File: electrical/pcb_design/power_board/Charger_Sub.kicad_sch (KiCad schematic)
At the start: 10 parts

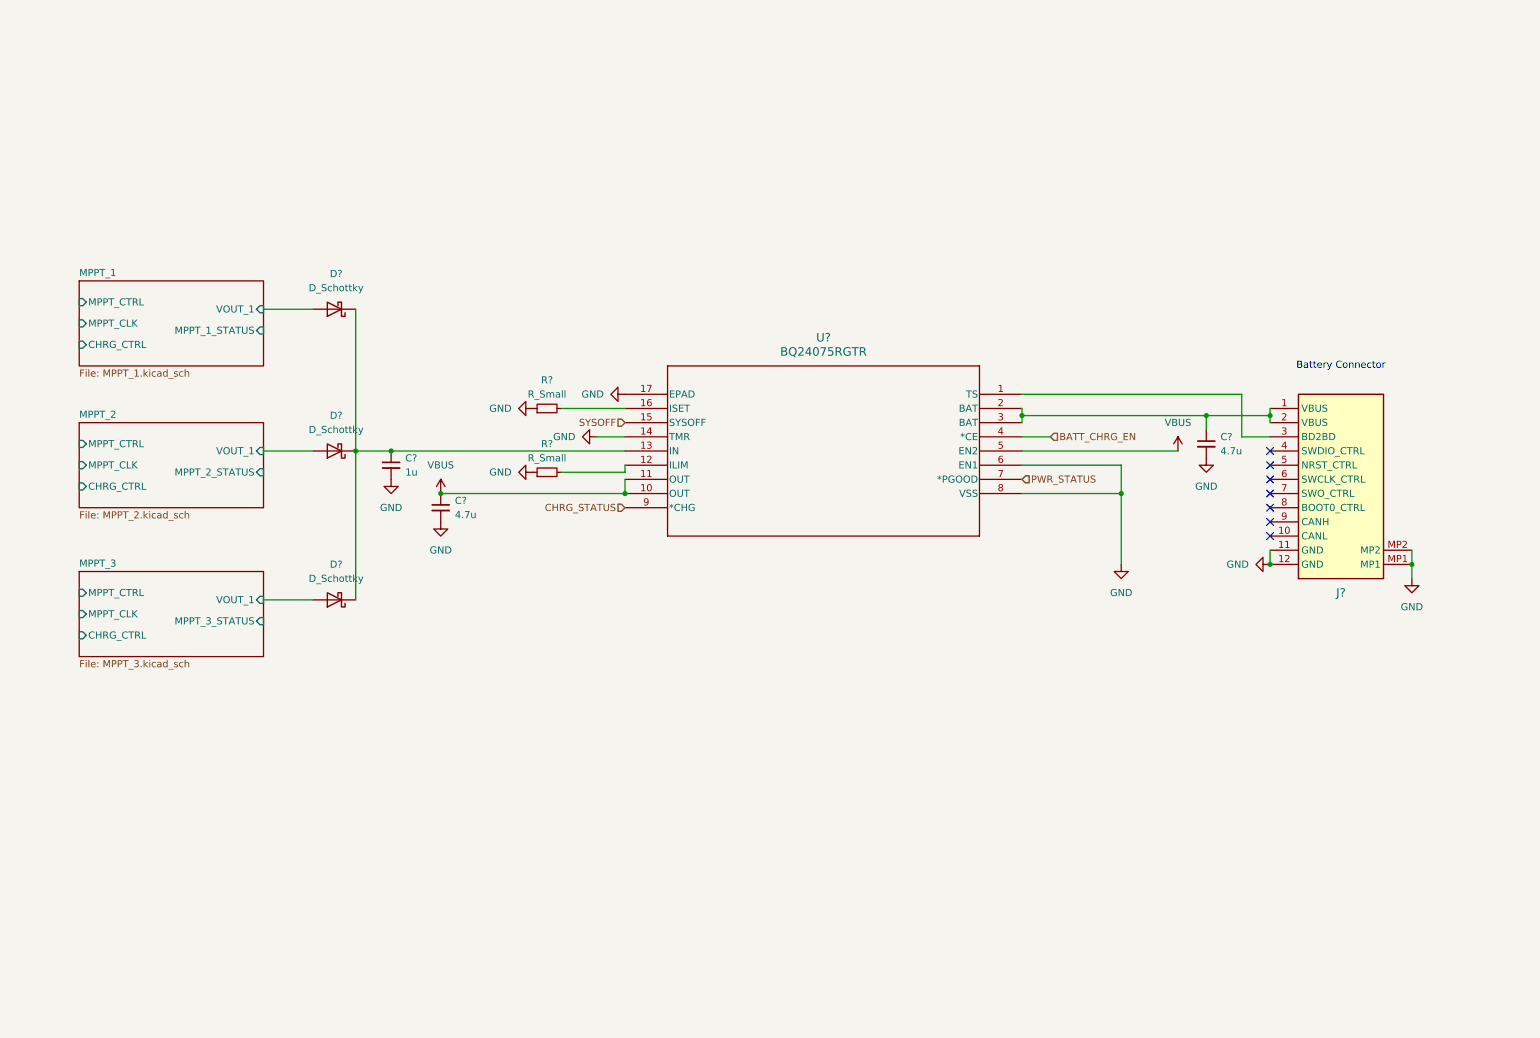
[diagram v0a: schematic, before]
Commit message: power board schematic first draft but missing some resistor and diode specs, and smart mcu pinout
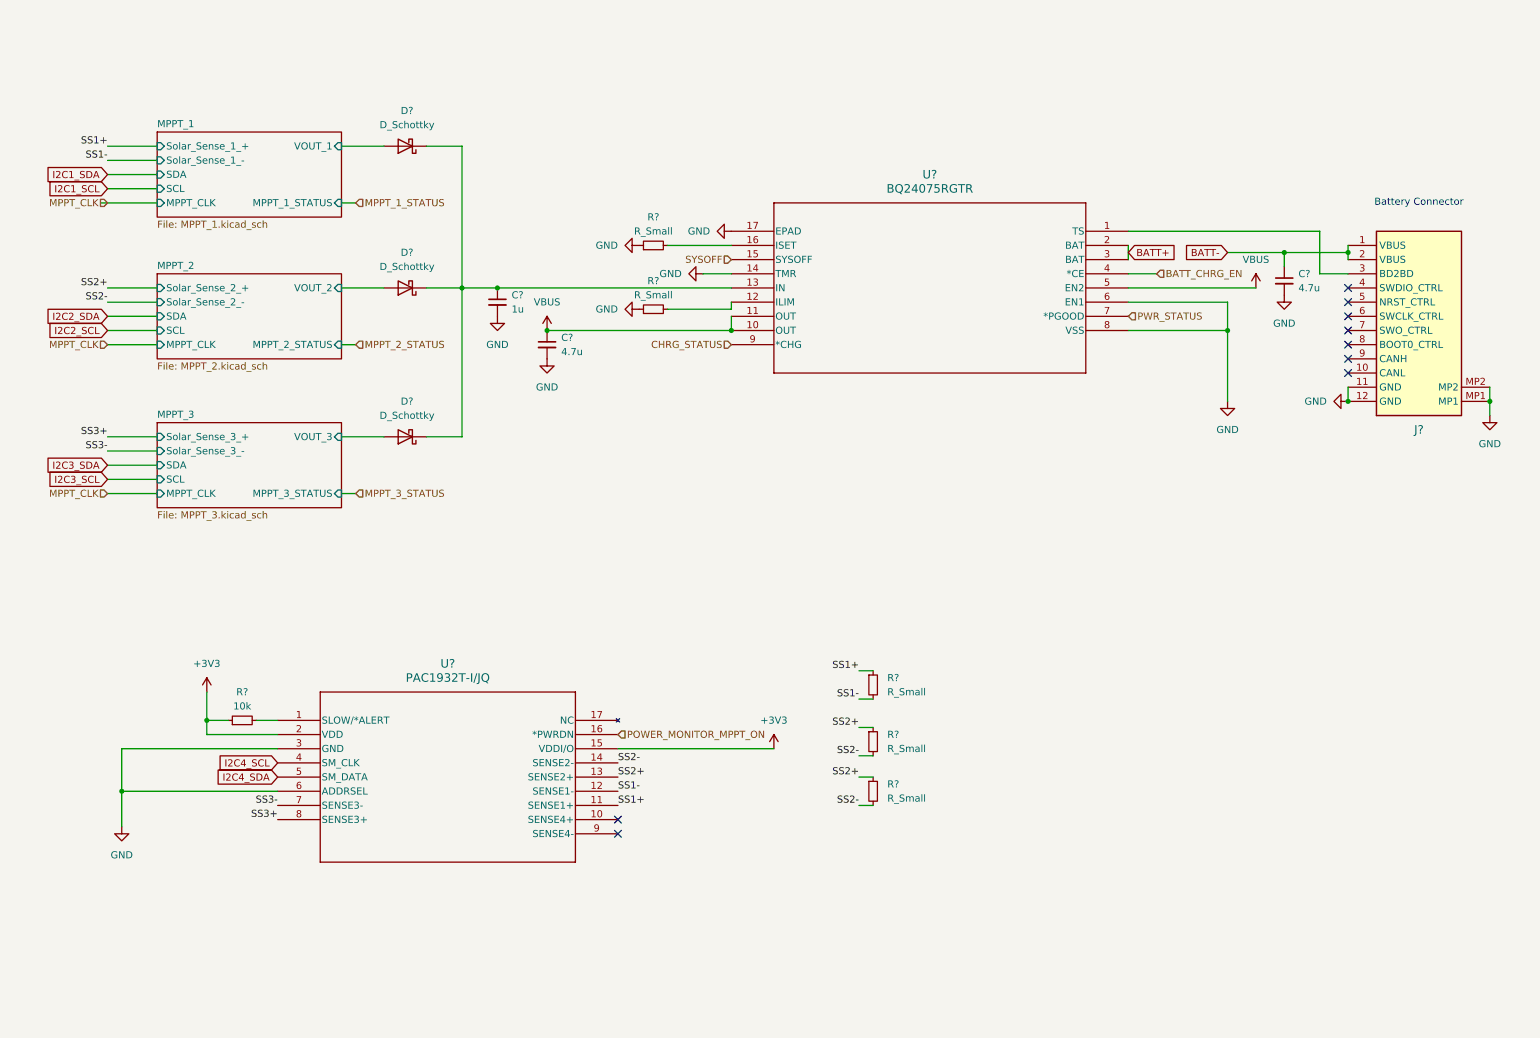
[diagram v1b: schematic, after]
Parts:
- removed D? (x2): D_Schottky, symbol Device:D_Schottky
- added D? (x2): D_Schottky, symbol Device:D_Schottky
- added R? (x3): R_Small, symbol Device:R_Small
- added R?: 10k, symbol Device:R_Small
- added U?: PAC1932T-I/JQ, UQFN16_JQ_MCH, symbol PAC1932:PAC1932T-I_JQ
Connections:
- net GND: now also U?.3 (GND), U?.6 (ADDRSEL)
- net at C?.1, D?.1 (K), U?.13 (IN): now also D?.1 (K), D?.1 (K)
- net BATT-: now reaches C?.1, J?.1 (VBUS), J?.2 (VBUS)
- net BATT-: no longer U?.2 (BAT), U?.3 (BAT)
- new net: R?.2, U?.1 (SLOW/*ALERT)
- new net +3V3: R?.1, U?.15 (VDDI/O), U?.2 (VDD)
- new net BATT+: U?.2 (BAT), U?.3 (BAT)
- new net I2C4_SCL: U?.4 (SM_CLK)
- new net I2C4_SDA: U?.5 (SM_DATA)
- new net MPPT_2/VOUT_2: D?.2 (A)
- new net MPPT_3/VOUT_3: D?.2 (A)
- new net POWER_MONITOR_MPPT_ON: U?.16 (*PWRDN)
- new net SS1+: R?.1, U?.11 (SENSE1+)
- new net SS1-: R?.2, U?.12 (SENSE1-)
- new net SS2+: R?.1, R?.1, U?.13 (SENSE2+)
- new net SS2-: R?.2, R?.2, U?.14 (SENSE2-)
- new net SS3+: U?.8 (SENSE3+)
- new net SS3-: U?.7 (SENSE3-)
- no-connect marks 7 -> 9
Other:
- sheet MPPT_1 ports: added SCL, SDA, Solar_Sense_1_+, Solar_Sense_1_-; removed CHRG_CTRL, MPPT_CTRL
- sheet MPPT_2 ports: added SCL, SDA, Solar_Sense_2_+, Solar_Sense_2_-, VOUT_2; removed CHRG_CTRL, MPPT_CTRL, VOUT_1
- sheet MPPT_3 ports: added SCL, SDA, Solar_Sense_3_+, Solar_Sense_3_-, VOUT_3; removed CHRG_CTRL, MPPT_CTRL, VOUT_1
- moved on the sheet: C?, D?, J?, R?, U?

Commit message: schematic review and some spec-ing
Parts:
- added R?: R_Small, symbol Device:R_Small
- added TP? (x4): ~, symbol Connector:TestPoint_Probe
- R?: value R_Small -> 1.18k
- R?: value R_Small -> 890
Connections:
- net POWER_MONITOR_MPPT_ON is gone; now on net +3V3: U?.16 (*PWRDN)
- net SYSOFF is gone; now on net GND: U?.15 (SYSOFF)
- net MPPT_1/VOUT_1: now also TP?.1
- net MPPT_2/VOUT_2: now also TP?.1
- net MPPT_3/VOUT_3: now also TP?.1
- net SS2+: no longer R?.1
- net SS2-: no longer R?.2
- net SS3+: now also R?.1
- net SS3-: now also R?.2
- net VBUS: now also U?.9 (SENSE4-), R?.2; no longer U?.10 (OUT), U?.11 (OUT)
- net at C?.1, D?.1 (K), D?.1 (K)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: now also TP?.1
- net Load+: now reaches U?.10 (SENSE4+)
- net Load+: now also U?.10 (OUT), U?.11 (OUT), R?.1
- no-connect marks 9 -> 7
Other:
- sheet MPPT_1 ports: added none; removed MPPT_CLK

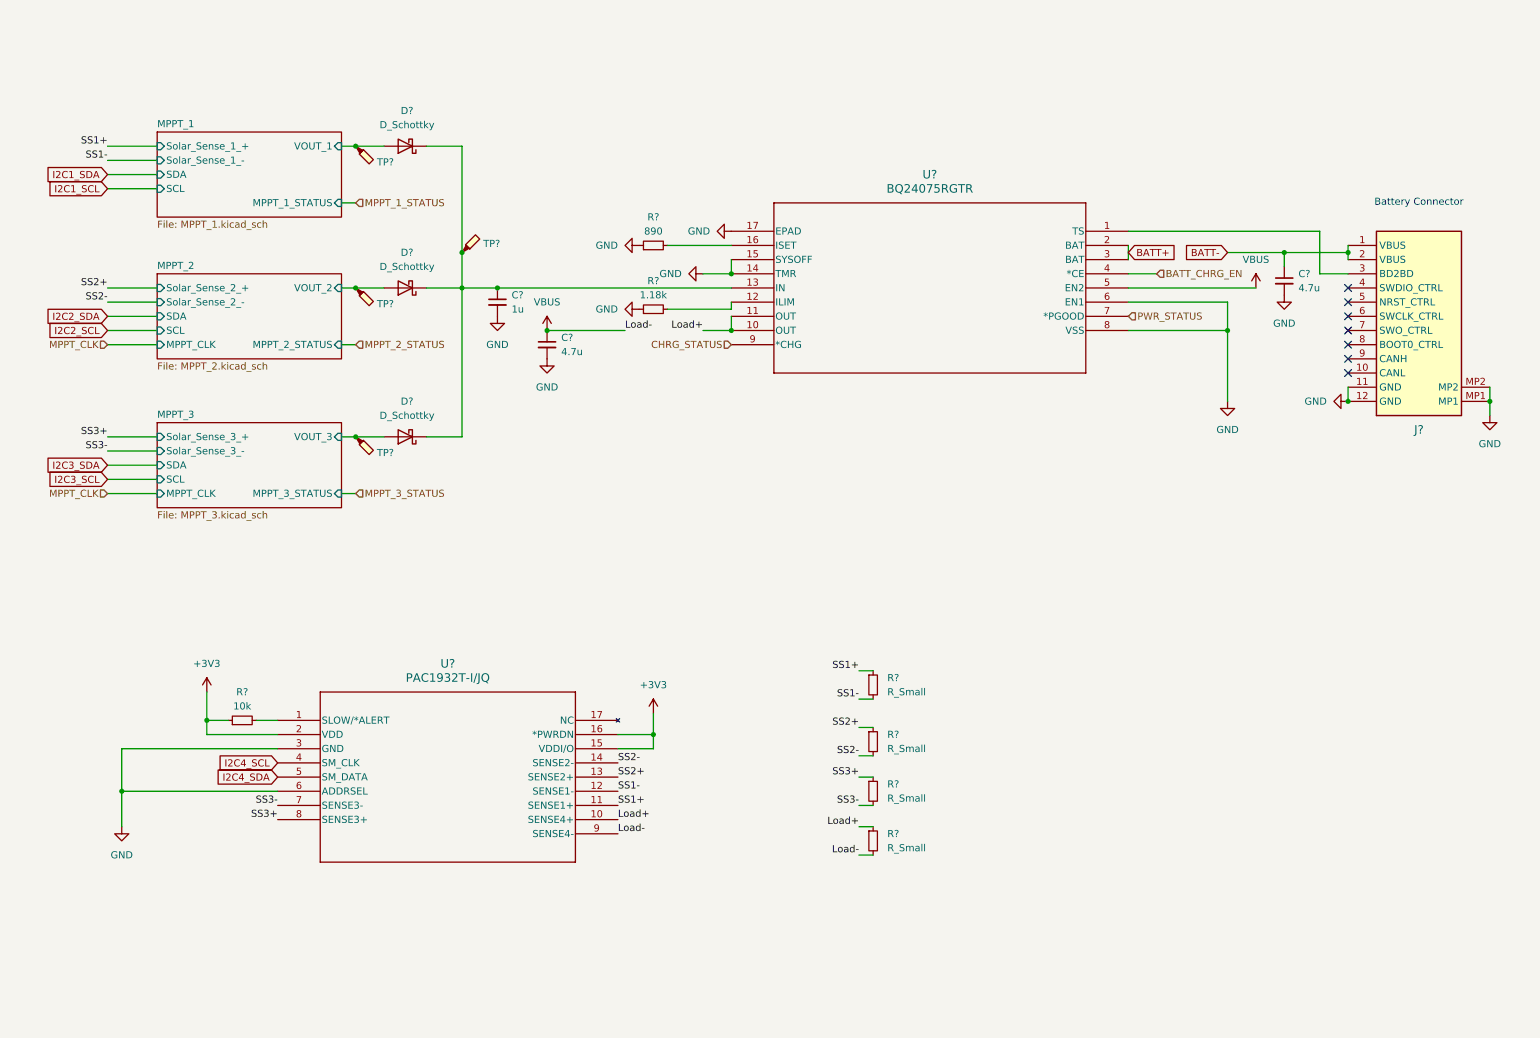
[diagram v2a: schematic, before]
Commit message: charger board, digipot on current pins of charger ic, voltage sensing on every side of solar panel
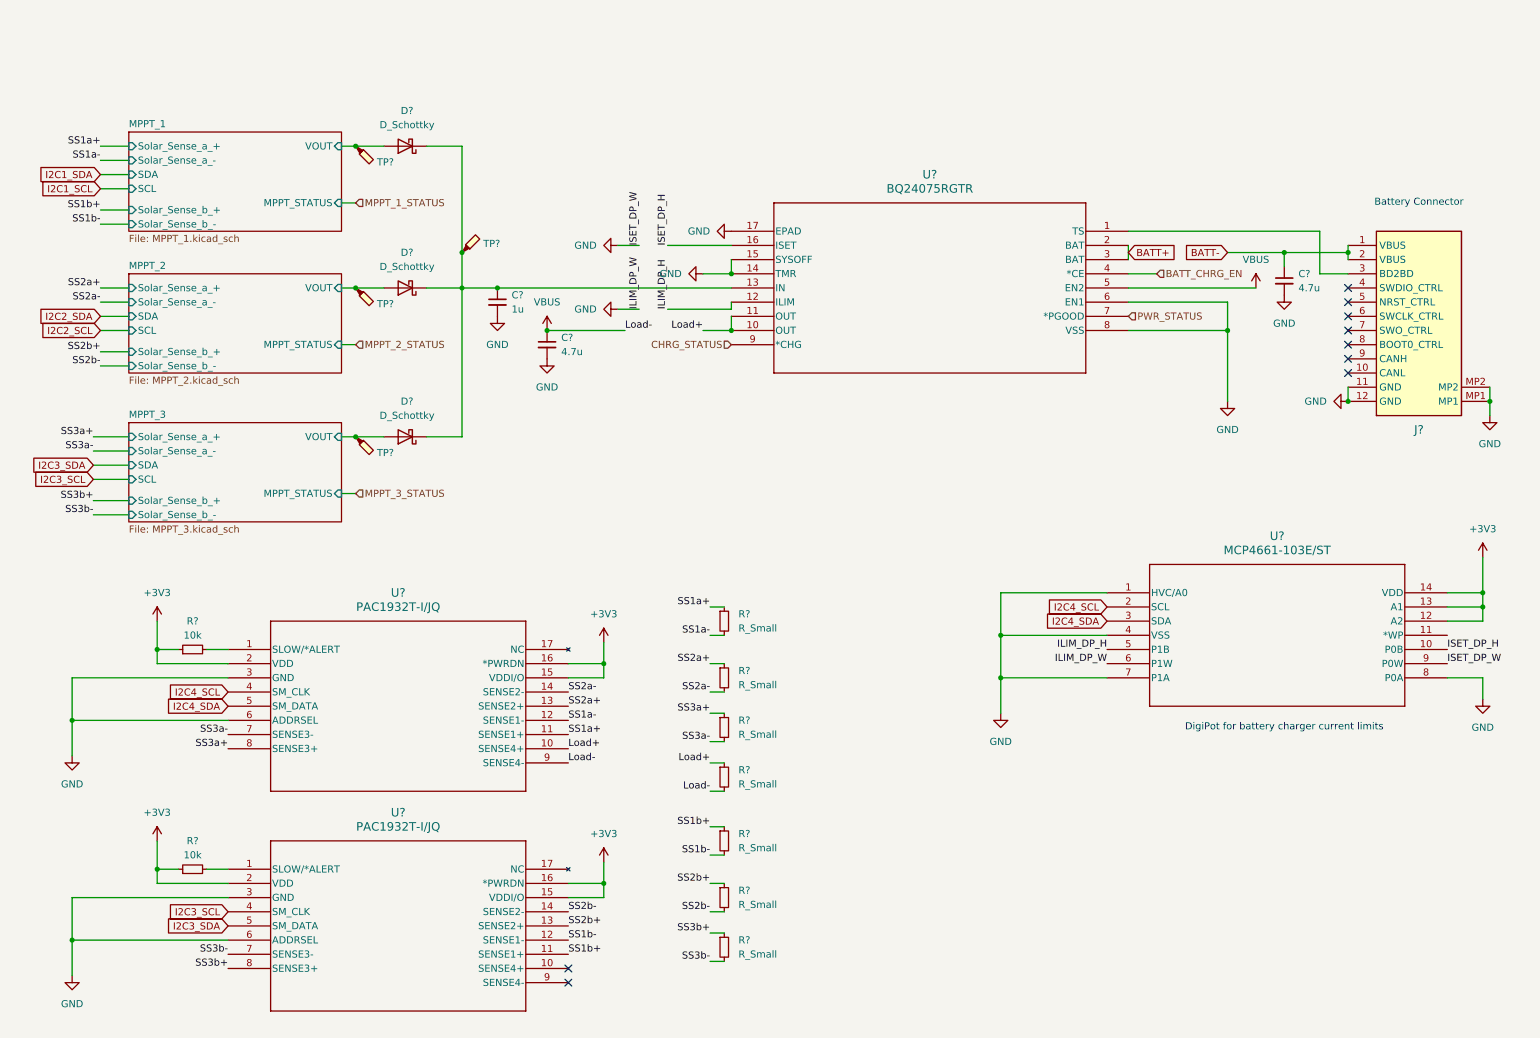
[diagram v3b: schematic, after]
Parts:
- removed R?: 1.18k, symbol Device:R_Small
- removed R?: 890, symbol Device:R_Small
- added R?: 10k, symbol Device:R_Small
- added R? (x3): R_Small, symbol Device:R_Small
- added U?: PAC1932T-I/JQ, UQFN16_JQ_MCH, symbol PAC1932:PAC1932T-I_JQ
- added U?: MCP4661-103E/ST, TSSOP14_MC_MCH, symbol MCP4661:MCP4661-103E_ST
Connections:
- net +3V3: now also R?.1, U?.12 (A2), U?.13 (A1), U?.14 (VDD), U?.15 (VDDI/O), U?.16 (*PWRDN), U?.2 (VDD)
- net GND: now also U?.1 (HVC/A0), U?.3 (GND), U?.4 (VSS), U?.6 (ADDRSEL), U?.6 (P1W), U?.7 (P1A), U?.8 (P0A), U?.9 (P0W)
- net I2C3_SCL: now also U?.4 (SM_CLK)
- net I2C3_SDA: now also U?.5 (SM_DATA)
- net I2C4_SCL: now also U?.2 (SCL)
- net I2C4_SDA: now also U?.3 (SDA)
- net ILIM_DP_H: now reaches U?.12 (ILIM)
- net ILIM_DP_H: now also U?.5 (P1B)
- net ISET_DP_H: now reaches U?.16 (ISET)
- net ISET_DP_H: now also U?.10 (P0B)
- net MPPT_1/VOUT_1 renamed MPPT_1/VOUT
- net MPPT_2/VOUT_2 renamed MPPT_2/VOUT
- net MPPT_3/VOUT_3 renamed MPPT_3/VOUT
- net SS1+ renamed SS1a+
- net SS1- renamed SS1a-
- net SS2+ renamed SS2a+
- net SS2- renamed SS2a-
- net SS3+ renamed SS3a+
- net SS3- renamed SS3a-
- new net: R?.2, U?.1 (SLOW/*ALERT)
- new net SS1b+: R?.1, U?.11 (SENSE1+)
- new net SS1b-: R?.2, U?.12 (SENSE1-)
- new net SS2b+: R?.1, U?.13 (SENSE2+)
- new net SS2b-: R?.2, U?.14 (SENSE2-)
- new net SS3b+: R?.1, U?.8 (SENSE3+)
- new net SS3b-: R?.2, U?.7 (SENSE3-)
- no-connect marks 7 -> 9
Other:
- sheet MPPT_1 ports: added MPPT_STATUS, Solar_Sense_a_+, Solar_Sense_a_-, Solar_Sense_b_+, Solar_Sense_b_-, VOUT; removed MPPT_1_STATUS, Solar_Sense_1_+, Solar_Sense_1_-, VOUT_1
- sheet MPPT_2 ports: added MPPT_STATUS, Solar_Sense_a_+, Solar_Sense_a_-, Solar_Sense_b_+, Solar_Sense_b_-, VOUT; removed MPPT_2_STATUS, MPPT_CLK, Solar_Sense_2_+, Solar_Sense_2_-, VOUT_2
- sheet MPPT_3 ports: added MPPT_STATUS, Solar_Sense_a_+, Solar_Sense_a_-, Solar_Sense_b_+, Solar_Sense_b_-, VOUT; removed MPPT_3_STATUS, MPPT_CLK, Solar_Sense_3_+, Solar_Sense_3_-, VOUT_3
- note added: "DigiPot for battery charger current limits"
- moved on the sheet: R?, U?

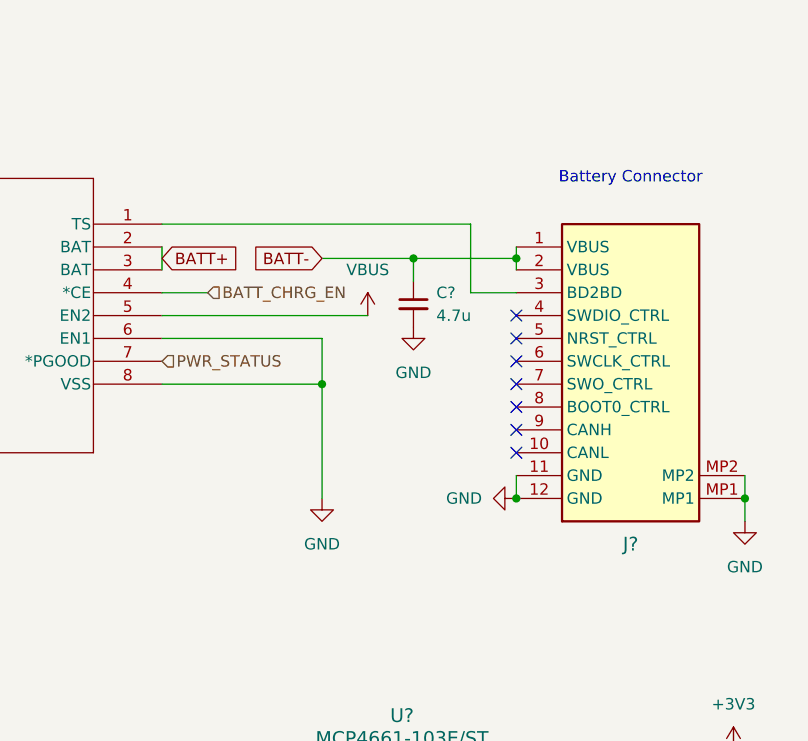
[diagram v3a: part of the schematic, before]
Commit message: replace battery connector, ts deactivated
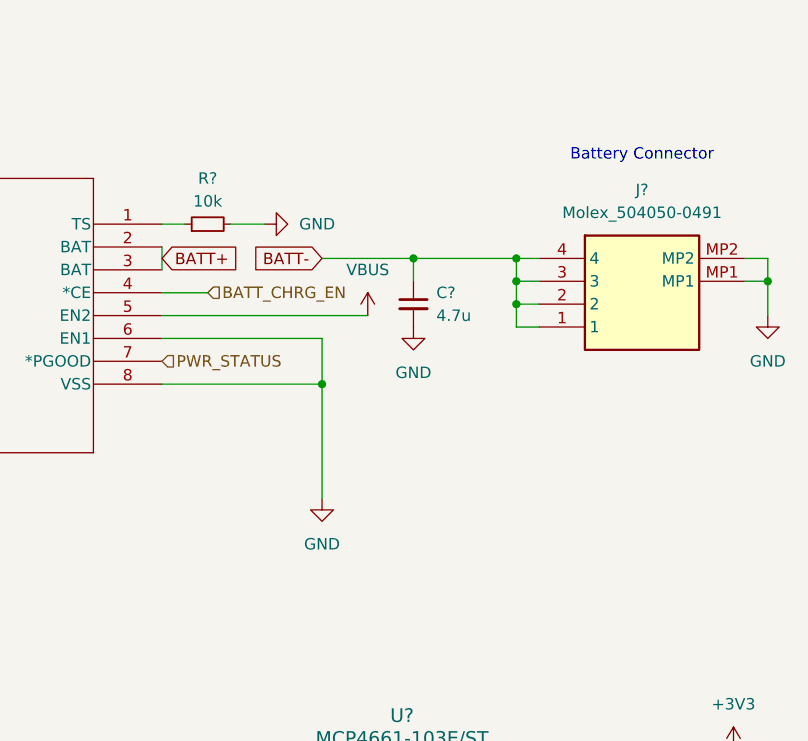
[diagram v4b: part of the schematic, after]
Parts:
- removed J?: Molex_504050-1291, footprints:Bus Connector (Control), symbol TVSC:Bus Connector (Control)
- added J?: Molex_504050-0491, footprints:Molex_504050-0491, symbol tvsc_symbols:Molex_504050-0491
- added R?: 10k, symbol Device:R_Small
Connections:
- net BATT-: now also J?.1, J?.2, J?.3, J?.4
- net GND: now also J?.MP1, J?.MP2, R?.2
- net at U?.1 (TS): now also R?.1
- no-connect marks 9 -> 2
